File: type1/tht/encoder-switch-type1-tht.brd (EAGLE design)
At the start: 25.6 x 21.6 mm, 9 parts

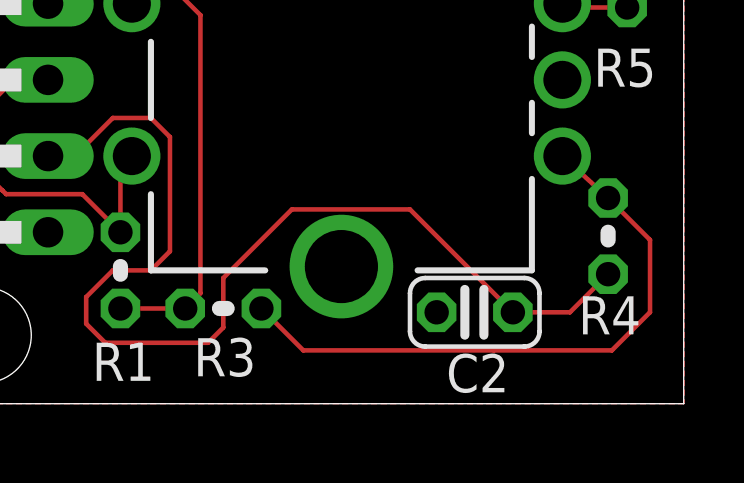
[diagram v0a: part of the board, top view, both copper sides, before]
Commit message: STEP files added, modified modules updated
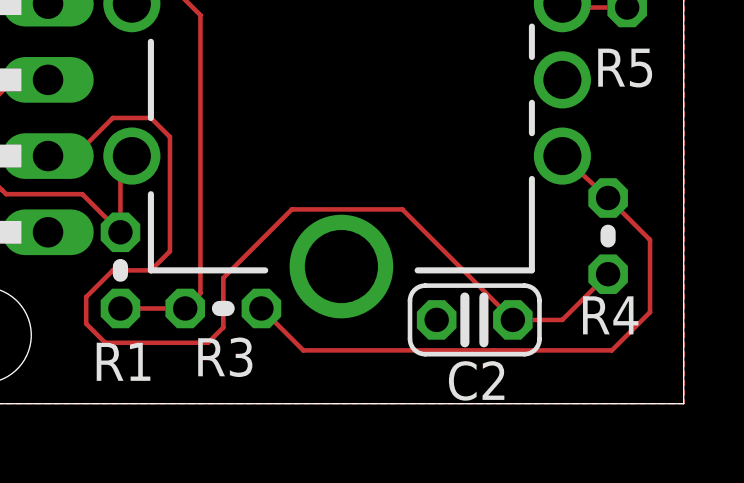
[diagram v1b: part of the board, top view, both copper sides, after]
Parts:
- C1, C2: device 001-private-inventory:C025-024X044 -> 006-rcl:C025-024X044
- R1, R2, R3, R4, R5: device 001-private-inventory:0204V -> 006-rcl:0204V
- moved C2 0.25 mm to (18.7, 2.79)
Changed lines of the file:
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@@
 <drawing>
 <settings>
-<setting alwaysvectorfont="no"/>
+<setting alwaysvectorfont="yes"/>
 <setting verticaltext="up"/>
 </settings>
@@
 </layers>
 <board>
+<fusionsync huburn="a.cGVyc29uYWw6dWUyYTlhNjVh" projecturn="a.cGVyc29uYWw6dWUyYTlhNjVhIzIwMTgwOTEwMTQ4MDIxNzUx" f3durn="urn:adsk.wipprod:dm.lineage:6lmDT7NKSX6VD5RqdL6YXw" pcbguid="18f5bb33-0175-4232-ad2f-581437e9251b" lastpulledtime="" lastsyncedchangeguid="dd832b6a-bee8-4bec-6a8b-2ffd538d46d8"/>
 <plain>
 <wire x1="0" y1="0" x2="25.634" y2="0" width="0" layer="20"/>
@@
 </autorouter>
 <elements>
-<element name="R1" library="001-private-inventory" package="0204V" package3d_urn="urn:adsk.eagle:package:23495/1" value="10K" x="6.858" y="4.445" rot="R90">
+<element name="R1" library="006-rcl" library_urn="urn:adsk.eagle:library:5746079" package="0204V" package3d_urn="urn:adsk.eagle:package:5803065/3" value="10K" x="6.858" y="4.445" rot="R90">
 <attribute name="NAME" x="8.001" y="2.032" size="1.27" layer="25" ratio="10" rot="R180"/>
 <attribute name="POWER" value="0.25-0.6 W" x="6.858" y="4.445" size="1.778" layer="27" rot="R90" display="off"/>
 <attribute name="SPICEPREFIX" value="R" x="6.858" y="4.445" size="1.778" layer="27" rot="R90" display="off"/>
 </element>
-<element name="R2" library="001-private-inventory" package="0204V" package3d_urn="urn:adsk.eagle:package:23495/1" value="4K7" x="9.779" y="18.288">
+<element name="R2" library="006-rcl" library_urn="urn:adsk.eagle:library:5746079" package="0204V" package3d_urn="urn:adsk.eagle:package:5803065/3" value="4K7" x="9.779" y="18.288">
 <attribute name="NAME" x="8.6614" y="19.4564" size="1.27" layer="25" ratio="10"/>
 <attribute name="POWER" value="0.25-0.6 W" x="9.779" y="18.288" size="1.778" layer="27" display="off"/>
 <attribute name="SPICEPREFIX" value="R" x="9.779" y="18.288" size="1.778" layer="27" display="off"/>
 </element>
-<element name="R3" library="001-private-inventory" package="0204V" package3d_urn="urn:adsk.eagle:package:23495/1" value="4K7" x="10.287" y="3.175">
+<element name="R3" library="006-rcl" library_urn="urn:adsk.eagle:library:5746079" package="0204V" package3d_urn="urn:adsk.eagle:package:5803065/3" value="4K7" x="10.287" y="3.175">
 <attribute name="NAME" x="9.2964" y="0.9144" size="1.27" layer="25" ratio="10"/>
 <attribute name="POWER" value="0.25-0.6 W" x="10.287" y="3.175" size="1.778" layer="27" display="off"/>
 <attribute name="SPICEPREFIX" value="R" x="10.287" y="3.175" size="1.778" layer="27" display="off"/>
 </element>
-<element name="C1" library="001-private-inventory" package="C025-024X044" package3d_urn="urn:adsk.eagle:package:23630/1" value="10nF" x="18.669" y="18.542" rot="R180">
+<element name="C1" library="006-rcl" library_urn="urn:adsk.eagle:library:5746079" package="C025-024X044" package3d_urn="urn:adsk.eagle:package:5815137/3" value="10nF" x="18.669" y="18.542" rot="R180">
 <attribute name="NAME" x="19.558" y="21.209" size="1.27" layer="25" ratio="10" rot="R180"/>
 <attribute name="SPICEPREFIX" value="C" x="18.669" y="18.542" size="1.778" layer="27" rot="R180" display="off"/>
 </element>
-<element name="C2" library="001-private-inventory" package="C025-024X044" package3d_urn="urn:adsk.eagle:package:23630/1" value="10nF" x="18.669" y="3.048" rot="R180">
-<attribute name="NAME" x="19.812" y="1.651" size="1.27" layer="25" ratio="10" rot="R180"/>
-<attribute name="SPICEPREFIX" value="C" x="18.669" y="3.048" size="1.778" layer="27" rot="R180" display="off"/>
-</element>
-<element name="R5" library="001-private-inventory" package="0204V" package3d_urn="urn:adsk.eagle:package:23495/1" value="82K" x="23.114" y="5.588" rot="R270">
+<element name="C2" library="006-rcl" library_urn="urn:adsk.eagle:library:5746079" package="C025-024X044" package3d_urn="urn:adsk.eagle:package:5815137/3" value="10nF" x="18.669" y="2.794" rot="R180">
+<attribute name="NAME" x="19.812" y="1.397" size="1.27" layer="25" ratio="10" rot="R180"/>
+<attribute name="SPICEPREFIX" value="C" x="18.669" y="2.794" size="1.778" layer="27" rot="R180" display="off"/>
+</element>
+<element name="R5" library="006-rcl" library_urn="urn:adsk.eagle:library:5746079" package="0204V" package3d_urn="urn:adsk.eagle:package:5803065/3" value="82K" x="23.114" y="5.588" rot="R270">
 <attribute name="NAME" x="22.6314" y="10.5664" size="1.27" layer="25" ratio="10"/>
 <attribute name="POWER" value="0.25-0.6 W" x="23.114" y="5.588" size="1.778" layer="27" rot="R270" display="off"/>
@@
 <attribute name="VALUE" x="2.667" y="9.525" size="0.6096" layer="27" font="vector" ratio="20" rot="R90"/>
 </element>
-<element name="R4" library="001-private-inventory" package="0204V" package3d_urn="urn:adsk.eagle:package:23495/1" value="82K" x="23.749" y="14.478" rot="R90">
+<element name="R4" library="006-rcl" library_urn="urn:adsk.eagle:library:5746079" package="0204V" package3d_urn="urn:adsk.eagle:package:5803065/3" value="82K" x="23.749" y="14.478" rot="R90">
 <attribute name="NAME" x="22.1234" y="2.3114" size="1.27" layer="25" ratio="10"/>
 <attribute name="POWER" value="0.25-0.6 W" x="23.749" y="14.478" size="1.778" layer="27" rot="R90" display="off"/>
@@
 <vertex x="0" y="0"/>
 </polygon>
+<wire x1="17.399" y1="2.794" x2="21.59" y2="10.795" width="0" layer="19" extent="1-1"/>
 </signal>
 <signal name="5V">
@@
 <contactref element="R5" pad="2"/>
 <contactref element="C2" pad="1"/>
-<wire x1="23.114" y1="4.318" x2="21.844" y2="3.048" width="0.1524" layer="1"/>
-<wire x1="21.844" y1="3.048" x2="19.939" y2="3.048" width="0.1524" layer="1"/>
+<wire x1="23.114" y1="4.318" x2="21.59" y2="2.794" width="0.1524" layer="1"/>
+<wire x1="21.59" y1="2.794" x2="19.939" y2="2.794" width="0.1524" layer="1"/>
 <contactref element="J2" pad="2"/>
 <wire x1="5.334" y1="8.255" x2="4.445" y2="8.255" width="0.1524" layer="1"/>
@@
 <wire x1="10.287" y1="4.191" x2="10.287" y2="2.54" width="0.1524" layer="1"/>
 <wire x1="12.573" y1="6.477" x2="10.287" y2="4.191" width="0.1524" layer="1"/>
-<wire x1="16.51" y1="6.477" x2="12.573" y2="6.477" width="0.1524" layer="1"/>
-<wire x1="19.939" y1="3.048" x2="16.51" y2="6.477" width="0.1524" layer="1"/>
+<wire x1="16.256" y1="6.477" x2="12.573" y2="6.477" width="0.1524" layer="1"/>
+<wire x1="19.939" y1="2.794" x2="16.256" y2="6.477" width="0.1524" layer="1"/>
 <wire x1="8.509" y1="8.89" x2="8.509" y2="5.08" width="0.1524" layer="1"/>
 <wire x1="9.779" y1="2.032" x2="6.35" y2="2.032" width="0.1524" layer="1"/>
@@
 </note>
 <note version="8.3" severity="warning">
+Since Version 8.3, EAGLE supports Fusion synchronisation.
+This feature will not be available in this version and saving
+the document will break the link to the Fusion PCB feature.
+</note>
+<note version="8.3" severity="warning">
